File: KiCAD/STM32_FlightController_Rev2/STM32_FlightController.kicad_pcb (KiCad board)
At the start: 4 copper layers, 42 x 44.4 mm, 71 parts, among them J1 USB_B_Micro, J11 GPS_V_{IN}, J12 GPS_TX, J13 GND, J14 GPS_RX, J15 ELRS_V_{IN}, J16 GND, J17 ELRS_TX, J18 ELRS_RX, J19 Conn_02x05_Odd_Even, J2 GND, J3 BAT, J4 CRT, J5 5V, J6 S1, J7 S2, J8 S3, J9 S4, Q1 IRLML6244, Q2 IRLML6244, SW1 PTS815SJM, SW2 SW_SPDT, U1 USBLC6-2SC6, U2 AMS1117-3.3, U3 TLV70018, U4 STM32F405RGTx, U5 BMP390L, U6 ICM-20948, Y1 8MHz

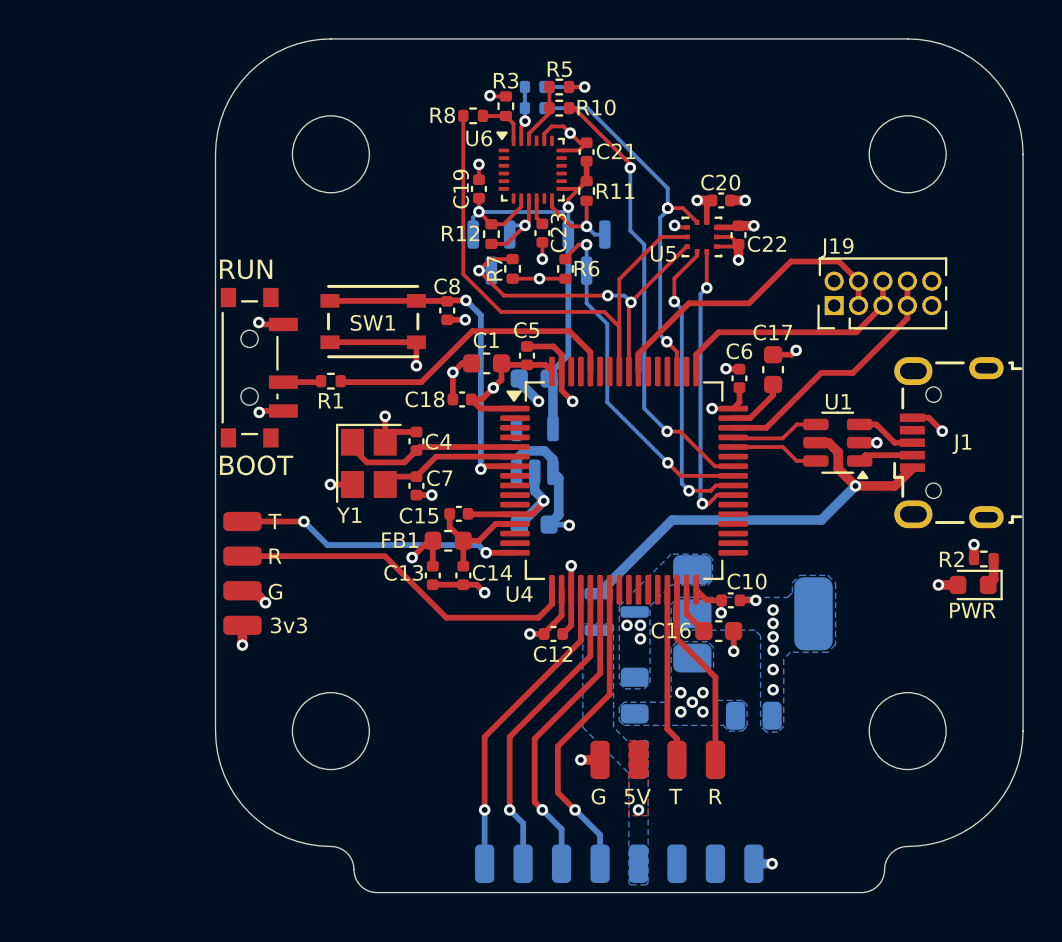
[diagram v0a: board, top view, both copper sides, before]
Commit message: corrected BMP390 schematic wiring and layout, among other corrections
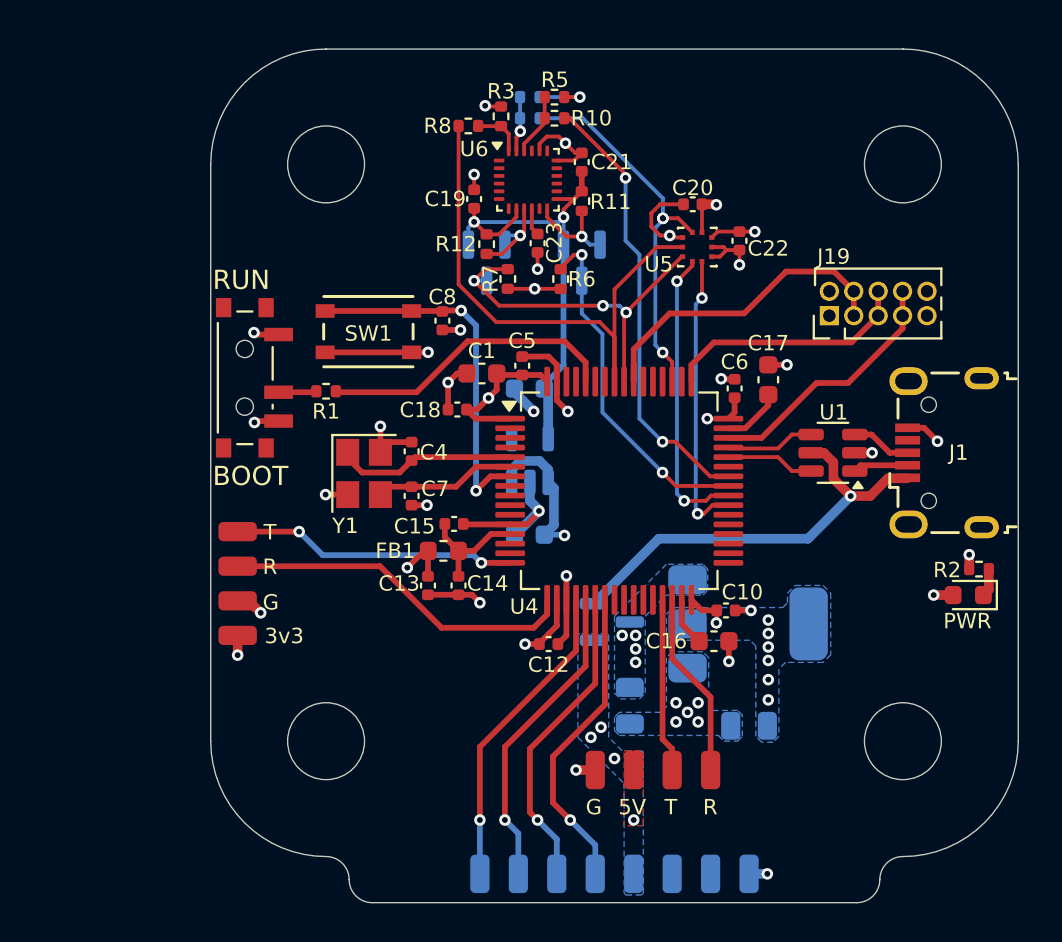
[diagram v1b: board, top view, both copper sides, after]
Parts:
- C3: value 1u -> 100n
- R10, R8, R9: value 4.7k -> 3.3k
- R3, R4, R5: value 4.7k -> 2.7k
- moved C20 1.49 mm to (118.8, 52.6), turned to 180 degrees
- moved C13 0.58 mm to (105.0, 72.4)
- moved C14 0.58 mm to (106.6, 72.4)
- moved C16 0.58 mm to (119.9, 75.3)
- moved C19 0.58 mm to (107.5, 52.3)
- moved C4 0.58 mm to (104.2, 65.5)
- moved D2 0.58 mm to (114.6, 74.3)
- moved FB1 0.58 mm to (105.8, 70.6)
- moved H3 0.58 mm to (99.8, 80.5)
- moved H4 0.58 mm to (129.8, 80.5)
- moved J1 0.58 mm to (131.9, 65.5)
- moved J11 0.58 mm to (95.2, 75.0)
- moved J12 0.58 mm to (95.2, 69.6)
- moved J15 0.58 mm to (115.8, 82.0)
- moved J16 0.58 mm to (113.8, 82.0)
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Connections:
- C22 pad 1: +3V3 -> Net-(U5-VDD)
- U5 pad 10: +3V3 -> Net-(U5-VDD)
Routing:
- net Net-(U5-VDD): track 0.00 -> 2.37 mm, vias 0 -> 1
- net GND: track 61.6 -> 63.7 mm, vias 35 -> 34
- net +3V3: track 37.1 -> 35.4 mm, vias 18 -> 17
- net /NRST: track 18.0 -> 18.9 mm
- net /V_MAIN: vias 3 -> 4
- net +5V: vias 1 -> 4

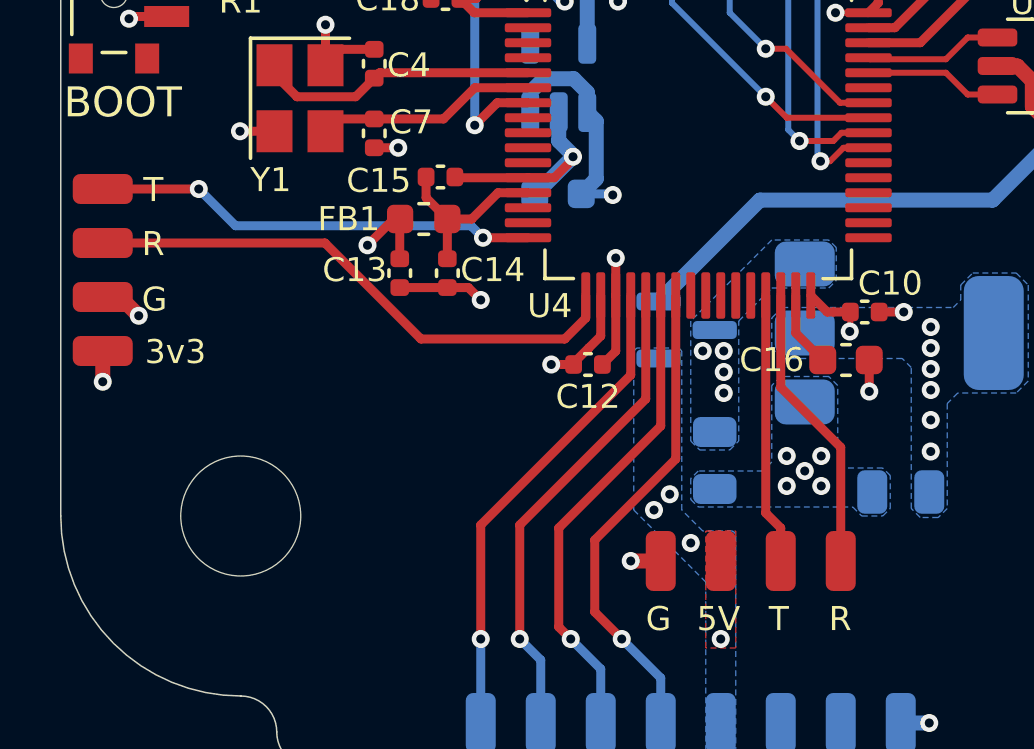
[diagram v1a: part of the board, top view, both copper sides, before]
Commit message: fixed respective RX and TX wirings
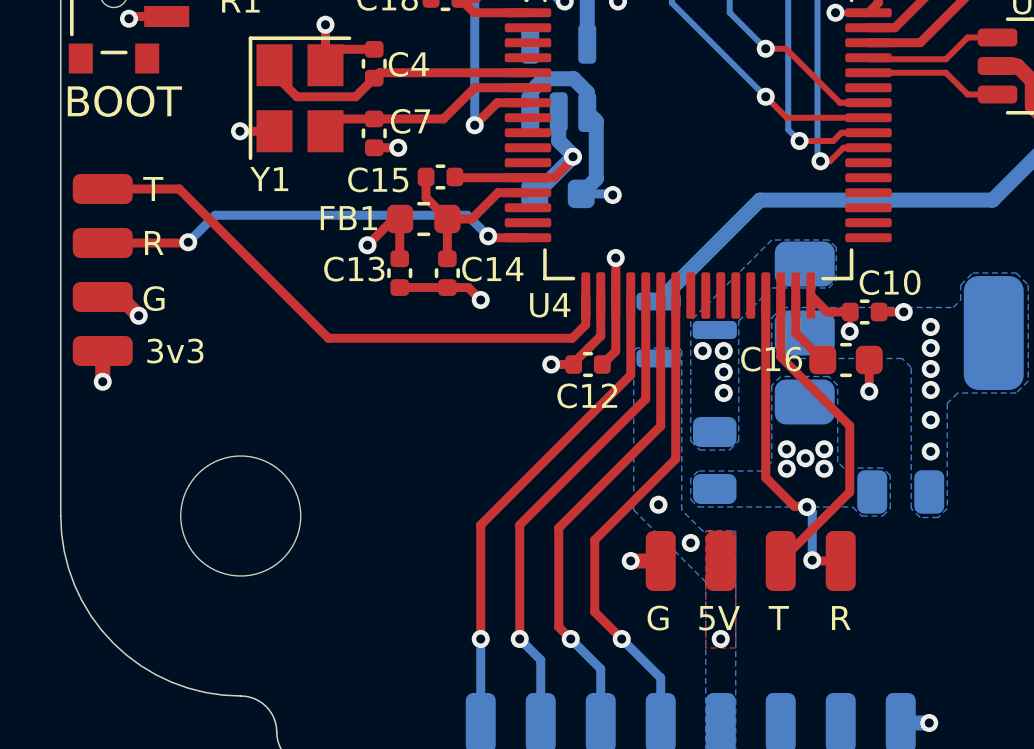
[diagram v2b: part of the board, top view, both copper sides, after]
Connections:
- U4 pad 16: /GPS_TX -> /GPS_RX
- U4 pad 17: /GPS_RX -> /GPS_TX
- U4 pad 29: /ELRS_TX -> /ELRS_RX
- U4 pad 30: /ELRS_RX -> /ELRS_TX
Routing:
- net /GPS_TX: track 14.8 -> 20.1 mm, vias 2 -> 0
- net /GPS_RX: track 18.5 -> 14.9 mm, vias 0 -> 2
- net /ELRS_TX: track 9.06 -> 10.8 mm
- net /ELRS_RX: track 9.68 -> 10.7 mm, vias 0 -> 2
- net +5V: vias 4 -> 3
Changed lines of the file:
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@@
 			(layers "F.Cu" "F.Mask" "F.Paste")
 			(roundrect_rratio 0.25)
-			(net 90 "/GPS_TX")
+			(net 91 "/GPS_RX")
 			(pinfunction "PA2")
 			(pintype "bidirectional")
@@
 			(layers "F.Cu" "F.Mask" "F.Paste")
 			(roundrect_rratio 0.25)
-			(net 91 "/GPS_RX")
+			(net 90 "/GPS_TX")
 			(pinfunction "PA3")
 			(pintype "bidirectional")
@@
 			(layers "F.Cu" "F.Mask" "F.Paste")
 			(roundrect_rratio 0.25)
-			(net 92 "/ELRS_TX")
+			(net 93 "/ELRS_RX")
 			(pinfunction "PB10")
 			(pintype "bidirectional")
@@
 			(layers "F.Cu" "F.Mask" "F.Paste")
 			(roundrect_rratio 0.25)
-			(net 93 "/ELRS_RX")
+			(net 92 "/ELRS_TX")
 			(pinfunction "PB11")
 			(pintype "bidirectional")
@@
 	)
 	(via
-		(at 117.95 78.525)
+		(at 117.95 78.3)
 		(size 0.6)
 		(drill 0.3)
@@
 	)
 	(via
-		(at 119.1 78.525)
+		(at 119.2 78.3)
 		(size 0.6)
 		(drill 0.3)
@@
 	)
 	(via
-		(at 118.55 79.025)
+		(at 118.575 78.6)
 		(size 0.6)
 		(drill 0.3)
@@
 	)
 	(via
-		(at 117.95 79.525)
-		(size 0.6)
-		(drill 0.3)
-		(layers "F.Cu" "B.Cu")
-		(free yes)
-		(net 1)
-	)
-	(via
 		(at 110.825 68.55)
 		(size 0.6)
@@
 	)
 	(via
+		(at 119.2 78.95)
+		(size 0.6)
+		(drill 0.3)
+		(layers "F.Cu" "B.Cu")
+		(free yes)
+		(net 1)
+	)
+	(via
 		(at 107.75 73.325)
 		(size 0.6)
@@
 	)
 	(via
-		(at 119.1 79.525)
+		(at 117.95 78.95)
 		(size 0.6)
 		(drill 0.3)
@@
 	)
 	(via
-		(at 114.05 79.8)
-		(size 0.6)
-		(drill 0.3)
-		(layers "F.Cu" "B.Cu")
-		(free yes)
-		(net 8)
-	)
-	(via
-		(at 113.525 80.325)
+		(at 113.675 80.15)
 		(size 0.6)
 		(drill 0.3)
@@
 	)
 	(segment
-		(start 107.825 71.25)
-		(end 109.325 71.25)
+		(start 97.7 69.625)
+		(end 102.675 74.6)
+		(width 0.3)
+		(layer "F.Cu")
+		(net 90)
+	)
+	(segment
+		(start 111.25 74.15)
+		(end 111.25 73.175)
 		(width 0.3)
 		(layer "F.Cu")
@@
 	(segment
 		(start 95.15 69.625)
-		(end 98.35 69.625)
+		(end 97.7 69.625)
+		(width 0.3)
+		(layer "F.Cu")
+		(net 90)
+	)
+	(segment
+		(start 102.675 74.6)
+		(end 110.8 74.6)
+		(width 0.3)
+		(layer "F.Cu")
+		(net 90)
+	)
+	(segment
+		(start 110.8 74.6)
+		(end 111.25 74.15)
+		(width 0.3)
+		(layer "F.Cu")
+		(net 90)
+	)
+	(segment
+		(start 111.25 73.925)
+		(end 111.25 73.175)
 		(width 0.3)
 		(layer "F.Cu")
 		(net 90)
 	)
+	(segment
+		(start 108.051 71.251)
+		(end 109.325 71.251)
+		(width 0.3)
+		(layer "F.Cu")
+		(net 91)
+	)
+	(segment
+		(start 95.15 71.425)
+		(end 97.975 71.425)
+		(width 0.3)
+		(layer "F.Cu")
+		(net 91)
+	)
+	(segment
+		(start 108 71.2)
+		(end 108.051 71.251)
+		(width 0.3)
+		(layer "F.Cu")
+		(net 91)
+	)
+	(segment
+		(start 97.975 71.425)
+		(end 98 71.4)
+		(width 0.3)
+		(layer "F.Cu")
+		(net 91)
+	)
 	(via
-		(at 107.825 71.25)
+		(at 108 71.2)
 		(size 0.6)
 		(drill 0.3)
 		(layers "F.Cu" "B.Cu")
-		(net 90)
+		(net 91)
 	)
 	(via
-		(at 98.35 69.625)
+		(at 98 71.4)
 		(size 0.6)
 		(drill 0.3)
 		(layers "F.Cu" "B.Cu")
-		(net 90)
+		(net 91)
 	)
 	(segment
-		(start 99.575 70.85)
-		(end 107.425 70.85)
+		(start 98 71.4)
+		(end 98.9 70.5)
 		(width 0.3)
 		(layer "B.Cu")
-		(net 90)
+		(net 91)
 	)
 	(segment
-		(start 98.35 69.625)
-		(end 99.575 70.85)
+		(start 107.3 70.5)
+		(end 108 71.2)
 		(width 0.3)
 		(layer "B.Cu")
-		(net 90)
+		(net 91)
 	)
 	(segment
-		(start 107.425 70.85)
-		(end 107.825 71.25)
+		(start 98.9 70.5)
+		(end 107.3 70.5)
 		(width 0.3)
 		(layer "B.Cu")
-		(net 90)
+		(net 91)
 	)
 	(segment
-		(start 102.55674 71.425)
-		(end 105.75674 74.625)
+		(start 117.75 75.220822)
+		(end 117.75 73.175)
 		(width 0.3)
 		(layer "F.Cu")
-		(net 91)
+		(net 92)
 	)
 	(segment
-		(start 95.15 71.425)
-		(end 102.55674 71.425)
+		(start 117.75 82.025)
+		(end 120.05 79.725)
 		(width 0.3)
 		(layer "F.Cu")
-		(net 91)
+		(net 92)
 	)
 	(segment
-		(start 110.55 74.625)
-		(end 111.25 73.925)
+		(start 120.05 79.725)
+		(end 120.05 77.520822)
 		(width 0.3)
 		(layer "F.Cu")
-		(net 91)
+		(net 92)
 	)
 	(segment
-		(start 105.75674 74.625)
-		(end 110.55 74.625)
+		(start 120.05 77.520822)
+		(end 117.75 75.220822)
 		(width 0.3)
 		(layer "F.Cu")
-		(net 91)
+		(net 92)
 	)
 	(segment
-		(start 111.25 73.925)
-		(end 111.25 73.175)
+		(start 117.25 79.25)
+		(end 117.25 73.175)
 		(width 0.3)
 		(layer "F.Cu")
-		(net 91)
+		(net 93)
 	)
 	(segment
-		(start 117.75 80.925)
-		(end 117.25 80.425)
+		(start 118.5 80.2)
+		(end 118.2 80.2)
 		(width 0.3)
 		(layer "F.Cu")
-		(net 92)
+		(net 93)
 	)
 	(segment
-		(start 117.25 80.425)
-		(end 117.25 73.175)
+		(start 118.525 80.225)
+		(end 118.5 80.2)
 		(width 0.3)
 		(layer "F.Cu")
-		(net 92)
+		(net 93)
 	)
 	(segment
-		(start 117.75 82.025)
-		(end 117.75 80.925)
+		(start 118.625 80.225)
+		(end 118.525 80.225)
 		(width 0.3)
 		(layer "F.Cu")
-		(net 92)
+		(net 93)
 	)
 	(segment
-		(start 117.75 73.175)
-		(end 117.75 76.235)
+		(start 118.2 80.2)
+		(end 117.25 79.25)
 		(width 0.3)
 		(layer "F.Cu")
@@
 	)
 	(segment
-		(start 117.75 76.235)
-		(end 119.75 78.235)
+		(start 119.75 82.025)
+		(end 118.825 82.025)
 		(width 0.3)
 		(layer "F.Cu")
@@
 	)
 	(segment
-		(start 119.75 78.235)
-		(end 119.75 82.025)
+		(start 118.825 82.025)
+		(end 118.8 82)
 		(width 0.3)
 		(layer "F.Cu")
 		(net 93)
 	)
+	(via
+		(at 118.8 82)
+		(size 0.6)
+		(drill 0.3)
+		(layers "F.Cu" "B.Cu")
+		(net 93)
+	)
+	(via
+		(at 118.625 80.225)
+		(size 0.6)
+		(drill 0.3)
+		(layers "F.Cu" "B.Cu")
+		(net 93)
+	)
+	(segment
+		(start 118.625 80.225)
+		(end 118.8 80.4)
+		(width 0.3)
+		(layer "B.Cu")
+		(net 93)
+	)
+	(segment
+		(start 118.8 80.4)
+		(end 118.8 82)
+		(width 0.3)
+		(layer "B.Cu")
+		(net 93)
+	)

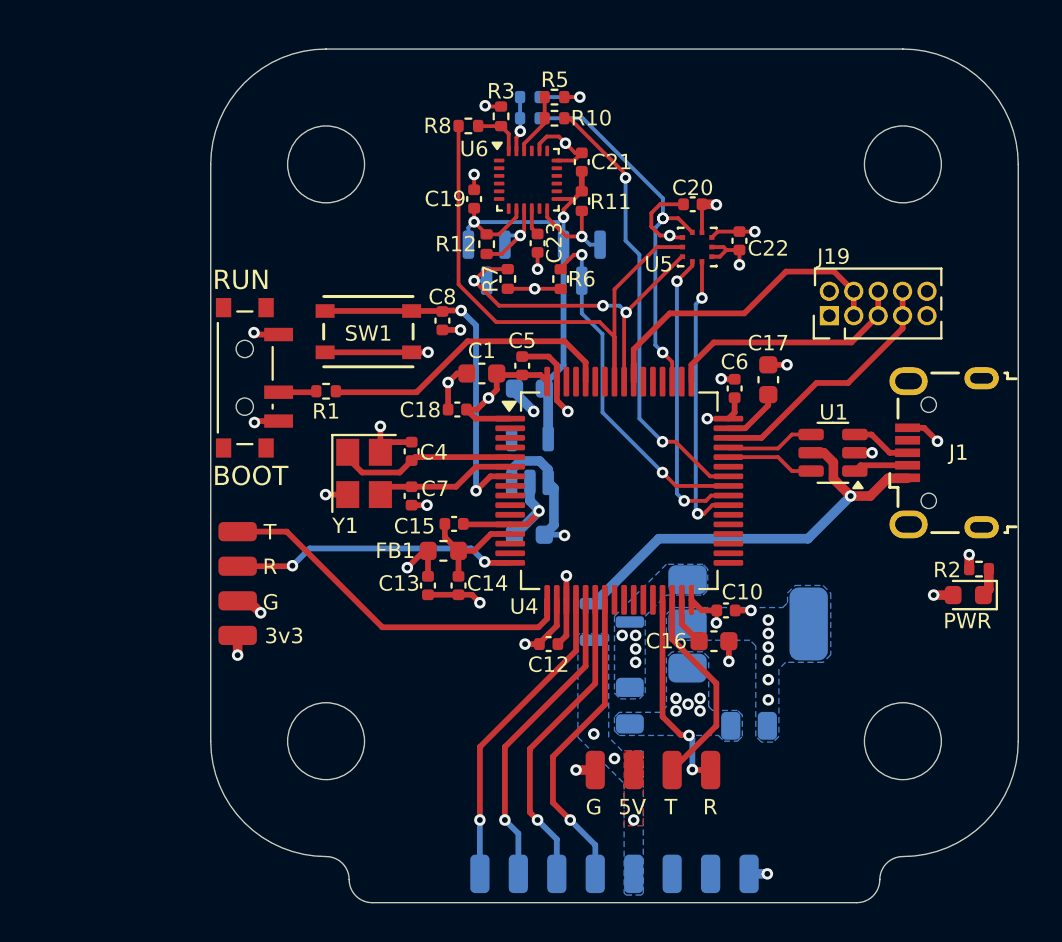
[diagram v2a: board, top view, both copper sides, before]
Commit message: correcting majority of via placements
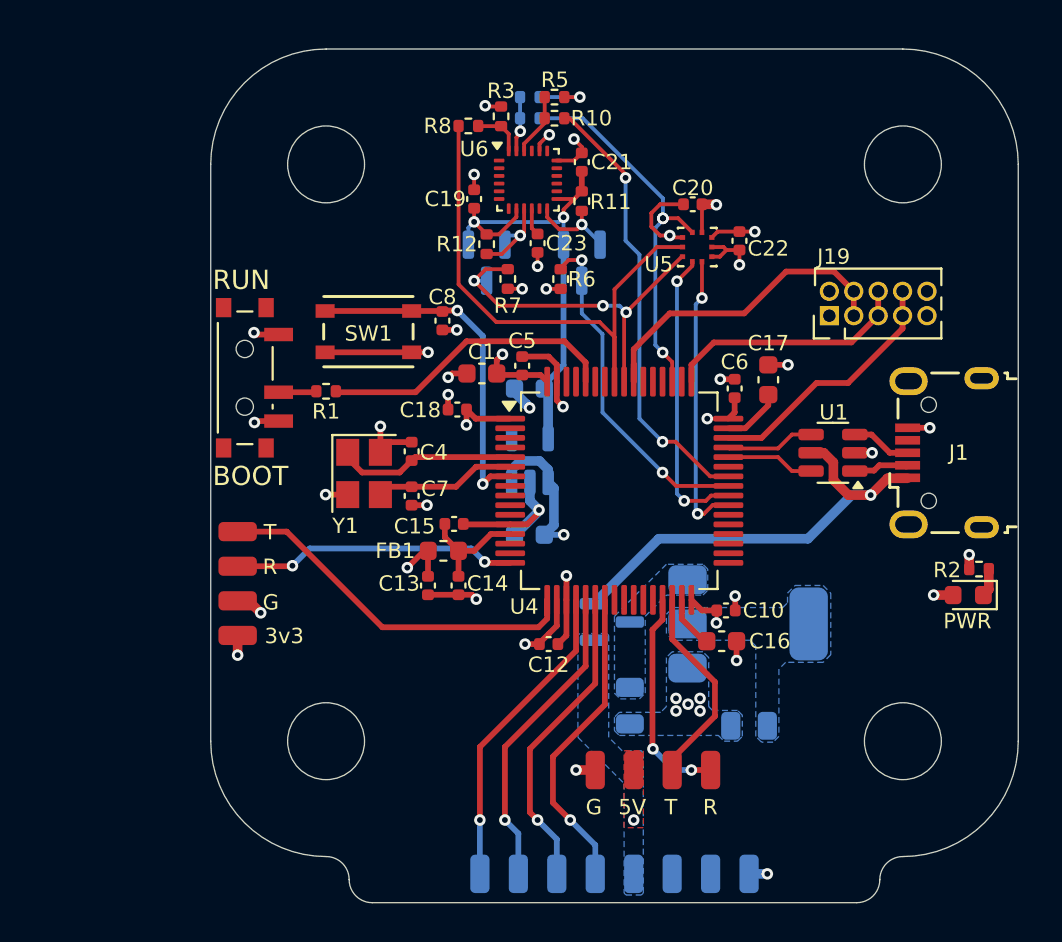
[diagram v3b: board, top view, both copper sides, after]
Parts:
- moved C16 0.40 mm to (120.3, 75.3)
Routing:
- net GND: track 63.7 -> 59.9 mm, vias 34 -> 36
- net +3V3: track 35.4 -> 33.2 mm, vias 17 -> 13
- net VBUS: track 22.6 -> 23.6 mm
- net /NRST: track 18.9 -> 18.1 mm
- net /ELRS_RX: track 10.7 -> 11.4 mm
- net /V_MAIN: vias 4 -> 0
- net +5V: vias 3 -> 1

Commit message: suggested fixes
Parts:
- added D3: PMEG6010CEH, Diode_SMD:D_SOD-123F, F.Cu at (85.8, 49.6)
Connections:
- C22 pad 1: Net-(U5-VDD) -> +3V3
- U5 pad 10: Net-(U5-VDD) -> +3V3
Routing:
- net +3V3: track 33.2 -> 36.6 mm
- net Net-(U5-VDD): track 2.37 -> 0.00 mm, vias 1 -> 0
